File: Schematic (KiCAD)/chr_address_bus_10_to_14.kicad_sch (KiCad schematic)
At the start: 80 parts

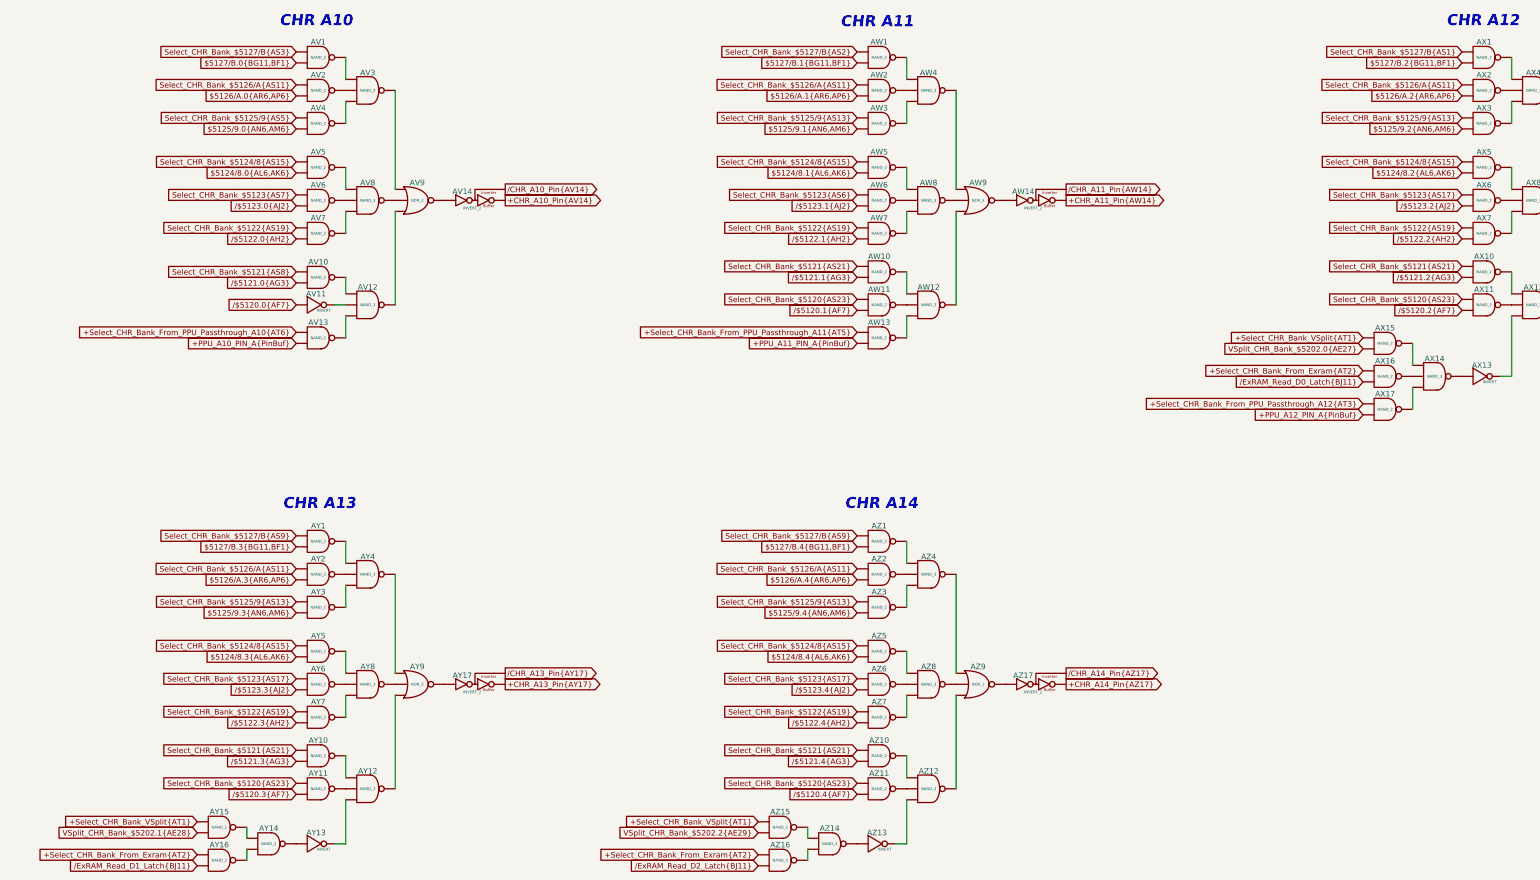
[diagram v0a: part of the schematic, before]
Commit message: - All cells in the left and center areas have now been added into the schematics.  - Changed naming of the PDF files; I was accidentally writing over furrtek's original with my new PDF.
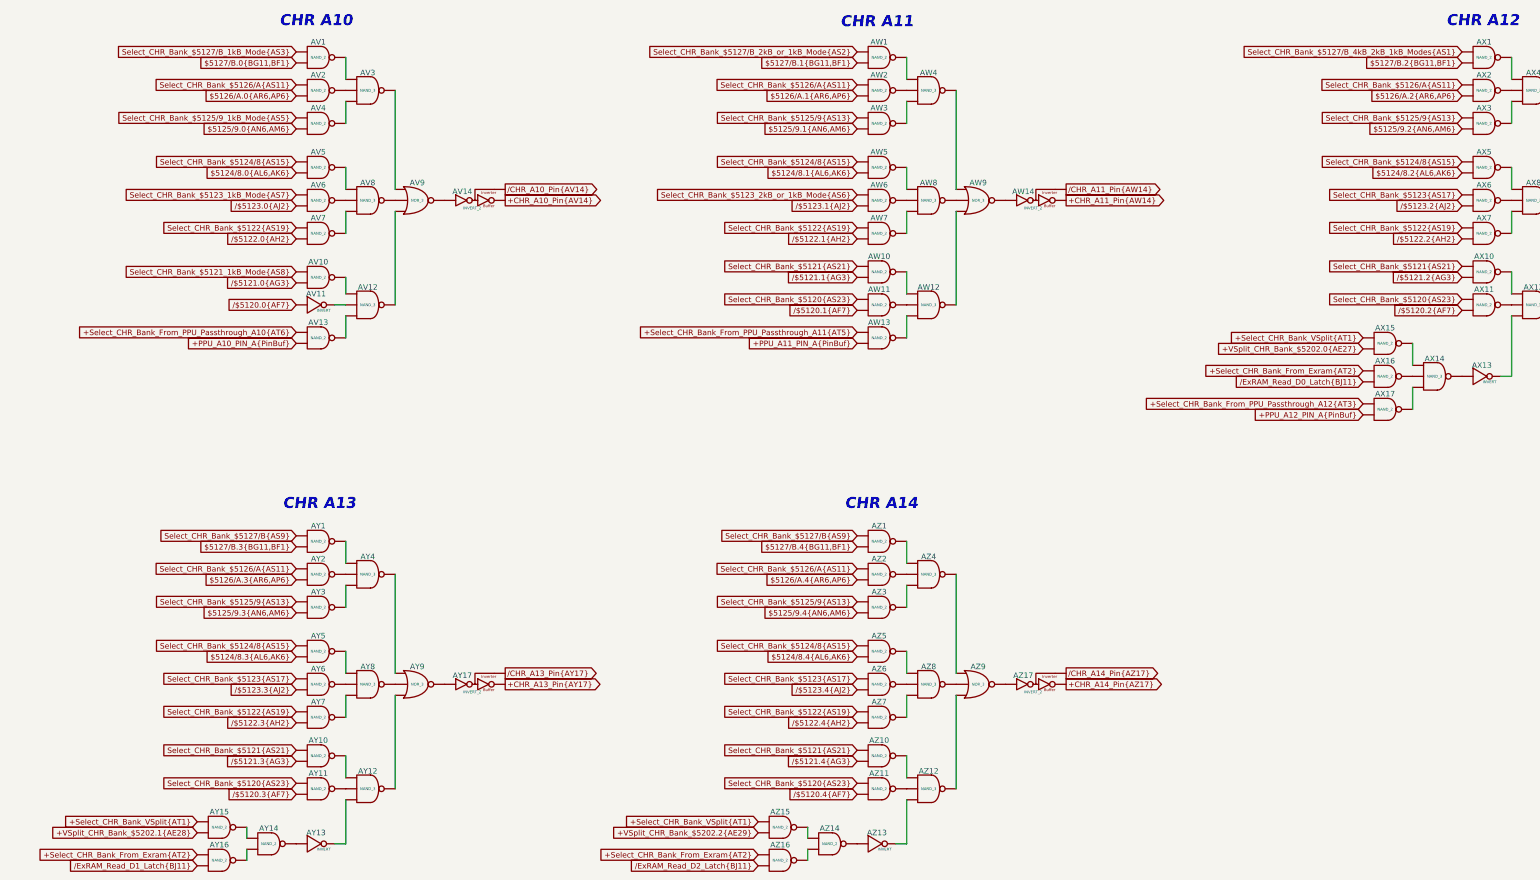
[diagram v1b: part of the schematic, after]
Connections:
- net Select_CHR_Bank_$5121{AS8} is gone; now on net /$5121.0{AG3}: AV10. (X)
- net Select_CHR_Bank_$5123{AS6} is gone; now on net /$5123.1{AJ2}: AW6. (X)
- net Select_CHR_Bank_$5123{AS7} is gone; now on net /$5123.0{AJ2}: AV6. (X)
- net Select_CHR_Bank_$5125/9{AS5} is gone; now on net Select_CHR_Bank_$5125/9_1kB_Mode{AS5}: AV4. (X)
- net Select_CHR_Bank_$5127/B{AS1} is gone; now on net Select_CHR_Bank_$5127/B_4kB_2kB_1kB_Modes{AS1}: AX1. (X)
- net Select_CHR_Bank_$5127/B{AS2} is gone; now on net Select_CHR_Bank_$5127/B_2kB_or_1kB_Mode{AS2}: AW1. (X)
- net VSplit_CHR_Bank_$5202.0{AE27} is gone; now on net +VSplit_CHR_Bank_$5202.0{AE27}: AX15. (X)
- net VSplit_CHR_Bank_$5202.2{AE29} is gone; now on net +VSplit_CHR_Bank_$5202.2{AE29}: AZ15. (X)
- net at AX8. (X): now also AX6. (X); no longer AX7. (X)
- net at AV3. (X): now also AV4. (X); no longer AV1. (X)
- net at AW8. (X): now also AW6. (X); no longer AW5. (X)
- net at AW12. (X): now also AW11. (X); no longer AW13. (X)
- net at AX4. (X): now also AX2. (X); no longer AX9. (X)
- net Select_CHR_Bank_$5127/B_4kB_2kB_1kB_Modes{AS1}: now reaches AX1. (X)
- net Select_CHR_Bank_$5127/B_4kB_2kB_1kB_Modes{AS1}: no longer AX4. (X)
- net at AZ14. (X): now also AZ13. (X); no longer AZ16. (X)
- net at AW9. (X): now also AW8. (X); no longer AW14. (X)
- net at AY8. (X): now also AY6. (X); no longer AY7. (X)
- net at AZ8. (X): now also AZ6. (X); no longer AZ5. (X)
- net at AY14. (X): now also AY13. (X); no longer AY15. (X)
- net at AY13. (X): now also AY12. (X); no longer AY14. (X)
- net at AX14. (X): now also AX17. (X); no longer AX16. (X)
- net at AX13. (X): now also AX12. (X); no longer AX14. (X)
- net +VSplit_CHR_Bank_$5202.0{AE27}: now reaches AX15. (X)
- net +VSplit_CHR_Bank_$5202.0{AE27}: no longer AX14. (X)
- net at AV9. (X): now also AV3. (X); no longer AV12. (X)
- net at AV8. (X): now also AV6. (X); no longer AV9. (X)
- net at AX12. (X): now also AX10. (X); no longer AX11. (X)
- net +VSplit_CHR_Bank_$5202.2{AE29}: now reaches AZ15. (X)
- net +VSplit_CHR_Bank_$5202.2{AE29}: no longer AZ14. (X)
- net at AZ13. (X): now also AZ12. (X); no longer AZ14. (X)
- net at AX9. (X): now also AX18. (X); no longer AX12. (X)
- net at AY4. (X): now also AY9. (X); no longer AY1. (X)
- net at AZ4. (X): now also AZ2. (X); no longer AZ3. (X)
- net at AZ9. (X): now also AZ17. (X); no longer AZ4. (X)
- net at AY9. (X): now also AY17. (X); no longer AY4. (X)
- net at AV12. (X): now also AV13. (X); no longer AV10. (X)
- net at AW4. (X): now also AW1. (X); no longer AW9. (X)
- net Select_CHR_Bank_$5125/9_1kB_Mode{AS5}: now reaches AV4. (X)
- net Select_CHR_Bank_$5125/9_1kB_Mode{AS5}: no longer AV3. (X)
- net Select_CHR_Bank_$5127/B_2kB_or_1kB_Mode{AS2}: now reaches AW1. (X)
- net Select_CHR_Bank_$5127/B_2kB_or_1kB_Mode{AS2}: no longer AW4. (X)
- net Select_CHR_Bank_$5127/B{AS3} renamed Select_CHR_Bank_$5127/B_1kB_Mode{AS3}
- net VSplit_CHR_Bank_$5202.1{AE28} renamed +VSplit_CHR_Bank_$5202.1{AE28}
- new net: AX7. (X), AX8. (X)
- new net: AV1. (X), AV3. (X)
- new net: AW5. (X), AW8. (X)
- new net: AW12. (X), AW13. (X)
- new net: AX4. (X), AX9. (X)
- new net: AX3. (X), AX4. (X)
- new net: AX1. (X), AX4. (X)
- new net: AZ14. (X), AZ16. (X)
- new net: AW14. (X), AW9. (X)
- new net: AY7. (X), AY8. (X)
- new net: AZ5. (X), AZ8. (X)
- new net: AW7. (X), AW8. (X)
- new net: AX5. (X), AX8. (X)
- new net: AY14. (X), AY15. (X)
- new net: AY14. (X), AY16. (X)
- new net: AX14. (X), AX16. (X)
- new net: AX13. (X), AX14. (X)
- new net: AX14. (X), AX15. (X)
- new net: AZ7. (X), AZ8. (X)
- new net: AV12. (X), AV9. (X)
- new net: AV8. (X), AV9. (X)
- new net: AV14. (X), AV9. (X)
- new net: AX11. (X), AX12. (X)
- new net: AZ14. (X), AZ15. (X)
- new net: AZ11. (X), AZ12. (X)
- new net: AX12. (X), AX9. (X)
- new net: AY1. (X), AY4. (X)
- new net: AZ3. (X), AZ4. (X)
- new net: AZ4. (X), AZ9. (X)
- new net: AZ1. (X), AZ4. (X)
- new net: AY3. (X), AY4. (X)
- new net: AY2. (X), AY4. (X)
- new net: AV10. (X), AV12. (X)
- new net: AV11. (X), AV12. (X)
- new net: AW12. (X), AW9. (X)
- new net: AW4. (X), AW9. (X)
- new net: AW10. (X), AW12. (X)
- new net: AX8. (X), AX9. (X)
- new net: AV7. (X), AV8. (X)
- new net: AY8. (X), AY9. (X)
- new net: AY5. (X), AY8. (X)
- new net: AV5. (X), AV8. (X)
- new net: AV2. (X), AV3. (X)
- new net: AY10. (X), AY12. (X)
- new net: AZ10. (X), AZ12. (X)
- new net: AW2. (X), AW4. (X)
- new net: AW3. (X), AW4. (X)
- new net: AZ12. (X), AZ9. (X)
- new net: AZ8. (X), AZ9. (X)
- new net: AY12. (X), AY9. (X)
- new net: AY11. (X), AY12. (X)
- new net Select_CHR_Bank_$5121_1kB_Mode{AS8}: AV10. (X)
- new net Select_CHR_Bank_$5123_1kB_Mode{AS7}: AV6. (X)
- new net Select_CHR_Bank_$5123_2kB_or_1kB_Mode{AS6}: AW6. (X)
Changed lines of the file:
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@@
 		)
 	)
-	(global_label "VSplit_CHR_Bank_$5202.1{AE28}"
+	(global_label "+VSplit_CHR_Bank_$5202.1{AE28}"
 		(shape input)
 		(at 52.07 210.82 180)
@@
 		)
 		(property "Intersheetrefs" "${INTERSHEET_REFS}"
-			(at 18.0608 210.82 0)
+			(at 16.4884 210.82 0)
 			(effects
 				(font
@@
 		)
 	)
-	(global_label "VSplit_CHR_Bank_$5202.2{AE29}"
+	(global_label "+VSplit_CHR_Bank_$5202.2{AE29}"
 		(shape input)
 		(at 181.61 210.82 180)
@@
 		)
 		(property "Intersheetrefs" "${INTERSHEET_REFS}"
-			(at 147.6008 210.82 0)
+			(at 146.0284 210.82 0)
 			(effects
 				(font
@@
 		)
 	)
-	(global_label "Select_CHR_Bank_$5121{AS8}"
+	(global_label "Select_CHR_Bank_$5121_1kB_Mode{AS8}"
 		(shape input)
 		(at 74.93 81.28 180)
@@
 		)
 		(property "Intersheetrefs" "${INTERSHEET_REFS}"
-			(at 43.4607 81.28 0)
+			(at 33.1799 81.28 0)
 			(effects
 				(font
@@
 		)
 	)
-	(global_label "Select_CHR_Bank_$5123{AS6}"
+	(global_label "Select_CHR_Bank_$5123_2kB_or_1kB_Mode{AS6}"
 		(shape input)
 		(at 204.47 63.5 180)
@@
 		)
 		(property "Intersheetrefs" "${INTERSHEET_REFS}"
-			(at 173.0007 63.5 0)
+			(at 155.3419 63.5 0)
 			(effects
 				(font
@@
 		)
 	)
-	(global_label "Select_CHR_Bank_$5127{slash}B{AS2}"
+	(global_label "Select_CHR_Bank_$5127{slash}B_2kB_or_1kB_Mode{AS2}"
 		(shape input)
 		(at 204.47 30.48 180)
@@
 		)
 		(property "Intersheetrefs" "${INTERSHEET_REFS}"
-			(at 170.4002 30.48 0)
+			(at 152.7414 30.48 0)
 			(effects
 				(font
@@
 		)
 	)
-	(global_label "Select_CHR_Bank_$5127{slash}B{AS1}"
+	(global_label "Select_CHR_Bank_$5127{slash}B_4kB_2kB_1kB_Modes{AS1}"
 		(shape input)
 		(at 344.17 30.48 180)
@@
 		)
 		(property "Intersheetrefs" "${INTERSHEET_REFS}"
-			(at 310.1002 30.48 0)
+			(at 289.8409 30.48 0)
 			(effects
 				(font
@@
 		)
 	)
-	(global_label "VSplit_CHR_Bank_$5202.0{AE27}"
+	(global_label "+VSplit_CHR_Bank_$5202.0{AE27}"
 		(shape input)
 		(at 321.31 99.06 180)
@@
 		)
 		(property "Intersheetrefs" "${INTERSHEET_REFS}"
-			(at 287.3008 99.06 0)
+			(at 285.7284 99.06 0)
 			(effects
 				(font
@@
 		)
 	)
-	(global_label "Select_CHR_Bank_$5125{slash}9{AS5}"
+	(global_label "Select_CHR_Bank_$5125{slash}9_1kB_Mode{AS5}"
 		(shape input)
 		(at 74.93 45.72 180)
@@
 		)
 		(property "Intersheetrefs" "${INTERSHEET_REFS}"
-			(at 40.9207 45.72 0)
+			(at 30.6399 45.72 0)
 			(effects
 				(font
@@
 		)
 	)
-	(global_label "Select_CHR_Bank_$5127{slash}B{AS3}"
+	(global_label "Select_CHR_Bank_$5127{slash}B_1kB_Mode{AS3}"
 		(shape input)
 		(at 74.93 30.48 180)
@@
 		)
 		(property "Intersheetrefs" "${INTERSHEET_REFS}"
-			(at 40.8602 30.48 0)
+			(at 30.5794 30.48 0)
 			(effects
 				(font
@@
 		)
 	)
-	(global_label "Select_CHR_Bank_$5123{AS7}"
+	(global_label "Select_CHR_Bank_$5123_1kB_Mode{AS7}"
 		(shape input)
 		(at 74.93 63.5 180)
@@
 		)
 		(property "Intersheetrefs" "${INTERSHEET_REFS}"
-			(at 43.4607 63.5 0)
-			(effects
-				(font
+			(at 33.1799 63.5 0)
+			(effects
+				(font
